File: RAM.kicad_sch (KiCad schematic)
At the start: 7 parts

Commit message: changed some ethernet stuff
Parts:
- gave numbers to parts that had none: 3
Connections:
- net USB0_D+: now also U1.A5 (USB_DP0)
- net USB0_D-: now also U1.B5 (USB_DM0)
- net USB1_D+: now also U1.B6 (USB_DP1)
- net USB1_D-: now also U1.B7 (USB_DM1)
- net USB2_D+: now also U1.A7 (USB_DP2)
- net USB2_D-: now also U1.A8 (USB_DM2)
- net USB3_D+: now also U1.B8 (USB_DP3)
- net USB3_D-: now also U1.B9 (USB_DM3)

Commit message: power things, minor changes
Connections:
- no-connect marks 10 -> 14
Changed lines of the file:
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@@
+	)
+	(no_connect
+		(at 54.61 138.43)
 	)
 	(no_connect
@@
 	)
 	(no_connect
+		(at 54.61 130.81)
+	)
+	(no_connect
 		(at 310.515 206.375)
+	)
+	(no_connect
+		(at 54.61 153.67)
 	)
 	(no_connect
@@
 	)
 	(no_connect
+		(at 54.61 208.28)
+	)
+	(no_connect

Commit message: minor changes
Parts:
- removed unit 7 of U1
- added C100, C101, C107, C108, C88, C89: 1uF, symbol Device:C
- added C102, C103, C104, C105, C109, C110, C111, C112, C113, C114, C115, C116, C117, C118, C119, C120, C121, C122, C90, C91, C92, C93, C94, C95, C96, C97, C98: 0.1uF, symbol Device:C
- added C106, C87, C99: 10uF, symbol Device:C
- added R20, R21: 2K, symbol Device:R
- added R22: 10)R, symbol Device:R
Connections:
- net GND: now also C100.2, C101.2, C102.2, C103.2, C104.2, C105.2, C106.2, C107.2, C108.2, C109.2, C110.2, C111.2, C112.2, C113.2, C114.2, C115.2, C116.2, C118.2, C119.2, C120.2, C121.2, C122.2, C87.2, C88.2, C89.2, C90.2, C91.2, C92.2, C93.2, C94.2, C95.2, C96.2, C97.2, C98.2, C99.2, R21.2
- net SCK_N: now also R22.2
- net SCK_P: now also R22.1
- net SVREF: now also C116.1, C117.2, C118.1, C119.1, C120.1, C121.1, C122.1, R20.2, R21.1
- net VCC1V5_DRAM: now also C100.1, C101.1, C102.1, C103.1, C104.1, C105.1, C106.1, C107.1, C108.1, C109.1, C110.1, C111.1, C112.1, C113.1, C114.1, C115.1, C117.1, C87.1, C88.1, C89.1, C90.1, C91.1, C92.1, C93.1, C94.1, C95.1, C96.1, C97.1, C98.1, C99.1, R20.1
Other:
- moved on the sheet: R1, R2, R3, U1C, U3, U4

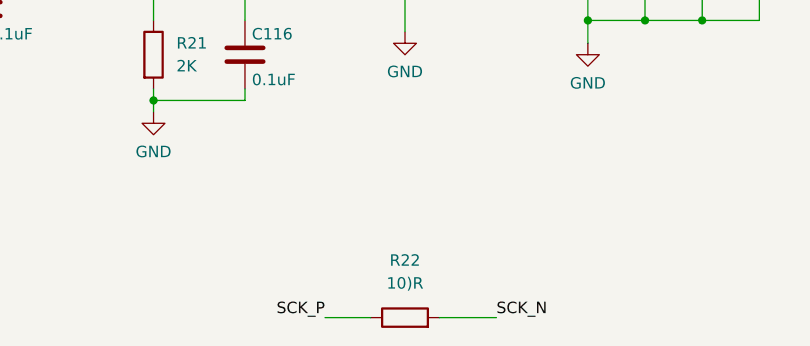
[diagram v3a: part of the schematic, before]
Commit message: linking symbols to footprints
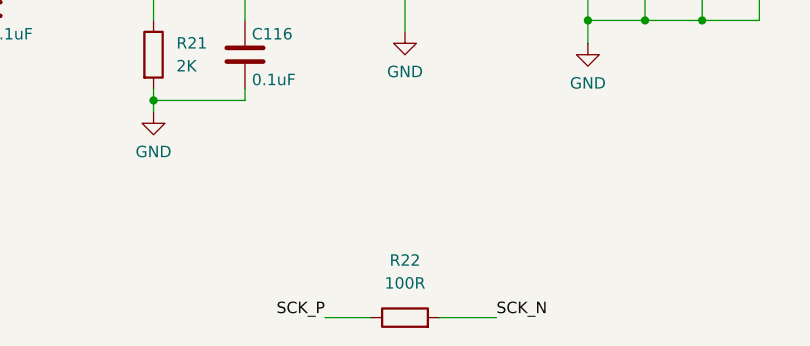
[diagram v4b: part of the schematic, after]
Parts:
- C100, C101, C107, C108, C88, C89: footprint (none) -> Capacitor_SMD:C_0402_1005Metric
- C102, C103, C104, C105, C106, C109, C110, C111, C112, C113, C114, C115, C116, C117, C118, C119, C120, C121, C122, C87, C90, C91, C92, C93, C94, C95, C96, C97, C98, C99: footprint (none) -> Capacitor_SMD:C_0603_1608Metric
- R1, R2, R20, R21, R3: footprint (none) -> Resistor_SMD:R_0402_1005Metric
- R22: value 10)R -> 100R; footprint (none) -> Resistor_SMD:R_0402_1005Metric
- U1: footprint BGA347_H3_AWT -> (none)
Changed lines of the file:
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@@
 			)
 		)
-		(property "Footprint" ""
+		(property "Footprint" "Resistor_SMD:R_0402_1005Metric"
 			(at 355.092 116.84 90)
 			(effects
@@
 			)
 		)
-		(property "Footprint" ""
+		(property "Footprint" "Capacitor_SMD:C_0603_1608Metric"
 			(at 194.0052 232.41 0)
 			(effects
@@
 			)
 		)
-		(property "Footprint" ""
+		(property "Footprint" "Capacitor_SMD:C_0603_1608Metric"
 			(at 337.5152 227.33 0)
 			(effects
@@
 			)
 		)
-		(property "Footprint" ""
+		(property "Footprint" "Capacitor_SMD:C_0603_1608Metric"
 			(at 331.1652 227.33 0)
 			(effects
@@
 			)
 		)
-		(property "Footprint" ""
+		(property "Footprint" "Capacitor_SMD:C_0603_1608Metric"
 			(at 244.8052 222.25 0)
 			(effects
@@
 			)
 		)
-		(property "Footprint" ""
+		(property "Footprint" "Capacitor_SMD:C_0402_1005Metric"
 			(at 50.4952 227.33 0)
 			(effects
@@
 			)
 		)
-		(property "Footprint" ""
+		(property "Footprint" "Capacitor_SMD:C_0603_1608Metric"
 			(at 238.4552 222.25 0)
 			(effects
@@
 			)
 		)
-		(property "Footprint" ""
+		(property "Footprint" "Capacitor_SMD:C_0603_1608Metric"
 			(at 305.7652 227.33 0)
 			(effects
@@
 			)
 		)
-		(property "Footprint" ""
+		(property "Footprint" "Capacitor_SMD:C_0603_1608Metric"
 			(at 56.8452 227.33 0)
 			(effects
@@
 			)
 		)
-		(property "Footprint" ""
+		(property "Footprint" "Resistor_SMD:R_0402_1005Metric"
 			(at 181.102 228.6 90)
 			(effects
@@
 			)
 		)
-		(property "Footprint" ""
+		(property "Footprint" "Capacitor_SMD:C_0603_1608Metric"
 			(at 107.6452 227.33 0)
 			(effects
@@
 			)
 		)
-		(property "Footprint" ""
+		(property "Footprint" "Capacitor_SMD:C_0603_1608Metric"
 			(at 101.2952 227.33 0)
 			(effects
@@
 			)
 		)
-		(property "Footprint" ""
+		(property "Footprint" "Capacitor_SMD:C_0603_1608Metric"
 			(at 324.8152 227.33 0)
 			(effects
@@
 			)
 		)
-		(property "Footprint" ""
+		(property "Footprint" "Capacitor_SMD:C_0603_1608Metric"
 			(at 251.1552 222.25 0)
 			(effects
@@
 			)
 		)
-		(property "Footprint" ""
+		(property "Footprint" "Capacitor_SMD:C_0603_1608Metric"
 			(at 312.1152 227.33 0)
 			(effects
@@
 			)
 		)
-		(property "Footprint" ""
+		(property "Footprint" "Capacitor_SMD:C_0603_1608Metric"
 			(at 88.5952 227.33 0)
 			(effects
@@
 			)
 		)
-		(property "Footprint" "BGA347_H3_AWT"
+		(property "Footprint" ""
 			(at 53.34 59.69 0)
 			(effects
@@
 			)
 		)
-		(property "Footprint" ""
+		(property "Footprint" "Capacitor_SMD:C_0603_1608Metric"
 			(at 164.7952 227.33 0)
 			(effects
@@
 			)
 		)
-		(property "Footprint" ""
+		(property "Footprint" "Capacitor_SMD:C_0603_1608Metric"
 			(at 82.2452 227.33 0)
 			(effects
@@
 			)
 		)
-		(property "Footprint" ""
+		(property "Footprint" "Resistor_SMD:R_0402_1005Metric"
 			(at 226.822 113.03 90)
 			(effects
@@
 			)
 		)
-		(property "Value" "10)R"
+		(property "Value" "100R"
 			(at 210.82 254 90)
 			(effects
@@
 			)
 		)
-		(property "Footprint" ""
+		(property "Footprint" "Resistor_SMD:R_0402_1005Metric"
 			(at 210.82 259.588 90)
 			(effects
@@
 			)
 		)
-		(property "Footprint" ""
+		(property "Footprint" "Capacitor_SMD:C_0603_1608Metric"
 			(at 63.1952 227.33 0)
 			(effects
@@
 			)
 		)
-		(property "Footprint" ""
+		(property "Footprint" "Capacitor_SMD:C_0402_1005Metric"
 			(at 44.1452 227.33 0)
 			(effects
@@
 			)
 		)
-		(property "Footprint" ""
+		(property "Footprint" "Capacitor_SMD:C_0402_1005Metric"
 			(at 299.4152 227.33 0)
 			(effects
@@
 			)
 		)
-		(property "Footprint" ""
+		(property "Footprint" "Capacitor_SMD:C_0603_1608Metric"
 			(at 211.7852 220.98 0)
 			(effects
@@
 			)
 		)
-		(property "Footprint" ""
+		(property "Footprint" "Capacitor_SMD:C_0603_1608Metric"
 			(at 75.8952 227.33 0)
 			(effects
@@
 			)
 		)
-		(property "Footprint" ""
+		(property "Footprint" "Resistor_SMD:R_0402_1005Metric"
 			(at 181.102 213.36 90)
 			(effects
@@
 			)
 		)
-		(property "Footprint" ""
+		(property "Footprint" "Capacitor_SMD:C_0603_1608Metric"
 			(at 343.8652 227.33 0)
 			(effects
@@
 			)
 		)
-		(property "Footprint" ""
+		(property "Footprint" "Capacitor_SMD:C_0603_1608Metric"
 			(at 194.0052 217.17 0)
 			(effects
@@
 			)
 		)
-		(property "Footprint" ""
+		(property "Footprint" "Capacitor_SMD:C_0603_1608Metric"
 			(at 158.4452 227.33 0)
 			(effects
@@
 			)
 		)
-		(property "Footprint" ""
+		(property "Footprint" "Capacitor_SMD:C_0603_1608Metric"
 			(at 318.4652 227.33 0)
 			(effects
@@
 			)
 		)
-		(property "Footprint" ""
+		(property "Footprint" "Capacitor_SMD:C_0603_1608Metric"
 			(at 232.1052 222.25 0)
 			(effects
@@
 			)
 		)
-		(property "Footprint" ""
+		(property "Footprint" "Capacitor_SMD:C_0603_1608Metric"
 			(at 286.7152 227.33 0)
 			(effects
@@
 			)
 		)
-		(property "Footprint" ""
+		(property "Footprint" "Capacitor_SMD:C_0603_1608Metric"
 			(at 126.6952 227.33 0)
 			(effects
@@
 			)
 		)
-		(property "Footprint" ""
+		(property "Footprint" "Capacitor_SMD:C_0402_1005Metric"
 			(at 133.0452 227.33 0)
 			(effects
@@
 			)
 		)
-		(property "Footprint" ""
+		(property "Footprint" "Capacitor_SMD:C_0603_1608Metric"
 			(at 152.0952 227.33 0)
 			(effects
@@
 			)
 		)
-		(property "Footprint" ""
+		(property "Footprint" "Resistor_SMD:R_0402_1005Metric"
 			(at 45.72 57.912 90)
 			(effects
@@
 			)
 		)
-		(property "Footprint" ""
+		(property "Footprint" "Capacitor_SMD:C_0603_1608Metric"
 			(at 145.7452 227.33 0)
 			(effects
@@
 			)
 		)
-		(property "Footprint" ""
+		(property "Footprint" "Capacitor_SMD:C_0603_1608Metric"
 			(at 94.9452 227.33 0)
 			(effects
@@
 			)
 		)
-		(property "Footprint" ""
+		(property "Footprint" "Capacitor_SMD:C_0402_1005Metric"
 			(at 139.3952 227.33 0)
 			(effects
@@
 			)
 		)
-		(property "Footprint" ""
+		(property "Footprint" "Capacitor_SMD:C_0402_1005Metric"
 			(at 293.0652 227.33 0)
 			(effects
@@
 			)
 		)
-		(property "Footprint" ""
+		(property "Footprint" "Capacitor_SMD:C_0603_1608Metric"
 			(at 37.7952 227.33 0)
 			(effects
@@
 			)
 		)
-		(property "Footprint" ""
+		(property "Footprint" "Capacitor_SMD:C_0603_1608Metric"
 			(at 69.5452 227.33 0)
 			(effects

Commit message: placed major components
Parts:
- C102, C103, C104, C105, C106, C109, C110, C111, C112, C113, C114, C115, C116, C117, C118, C119, C120, C121, C122, C87, C90, C91, C92, C93, C94, C95, C96, C97, C98, C99: footprint Capacitor_SMD:C_0603_1608Metric -> Capacitor_SMD:C_0402_1005Metric
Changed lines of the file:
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@@
 			)
 		)
-		(property "Footprint" "Capacitor_SMD:C_0603_1608Metric"
+		(property "Footprint" "Capacitor_SMD:C_0402_1005Metric"
 			(at 194.0052 232.41 0)
 			(effects
@@
 			)
 		)
-		(property "Footprint" "Capacitor_SMD:C_0603_1608Metric"
+		(property "Footprint" "Capacitor_SMD:C_0402_1005Metric"
 			(at 337.5152 227.33 0)
 			(effects
@@
 			)
 		)
-		(property "Footprint" "Capacitor_SMD:C_0603_1608Metric"
+		(property "Footprint" "Capacitor_SMD:C_0402_1005Metric"
 			(at 331.1652 227.33 0)
 			(effects
@@
 			)
 		)
-		(property "Footprint" "Capacitor_SMD:C_0603_1608Metric"
+		(property "Footprint" "Capacitor_SMD:C_0402_1005Metric"
 			(at 244.8052 222.25 0)
 			(effects
@@
 			)
 		)
-		(property "Footprint" "Capacitor_SMD:C_0603_1608Metric"
+		(property "Footprint" "Capacitor_SMD:C_0402_1005Metric"
 			(at 238.4552 222.25 0)
 			(effects
@@
 			)
 		)
-		(property "Footprint" "Capacitor_SMD:C_0603_1608Metric"
+		(property "Footprint" "Capacitor_SMD:C_0402_1005Metric"
 			(at 305.7652 227.33 0)
 			(effects
@@
 			)
 		)
-		(property "Footprint" "Capacitor_SMD:C_0603_1608Metric"
+		(property "Footprint" "Capacitor_SMD:C_0402_1005Metric"
 			(at 56.8452 227.33 0)
 			(effects
@@
 			)
 		)
-		(property "Footprint" "Capacitor_SMD:C_0603_1608Metric"
+		(property "Footprint" "Capacitor_SMD:C_0402_1005Metric"
 			(at 107.6452 227.33 0)
 			(effects
@@
 			)
 		)
-		(property "Footprint" "Capacitor_SMD:C_0603_1608Metric"
+		(property "Footprint" "Capacitor_SMD:C_0402_1005Metric"
 			(at 101.2952 227.33 0)
 			(effects
@@
 			)
 		)
-		(property "Footprint" "Capacitor_SMD:C_0603_1608Metric"
+		(property "Footprint" "Capacitor_SMD:C_0402_1005Metric"
 			(at 324.8152 227.33 0)
 			(effects
@@
 			)
 		)
-		(property "Footprint" "Capacitor_SMD:C_0603_1608Metric"
+		(property "Footprint" "Capacitor_SMD:C_0402_1005Metric"
 			(at 251.1552 222.25 0)
 			(effects
@@
 			)
 		)
-		(property "Footprint" "Capacitor_SMD:C_0603_1608Metric"
+		(property "Footprint" "Capacitor_SMD:C_0402_1005Metric"
 			(at 312.1152 227.33 0)
 			(effects
@@
 			)
 		)
-		(property "Footprint" "Capacitor_SMD:C_0603_1608Metric"
+		(property "Footprint" "Capacitor_SMD:C_0402_1005Metric"
 			(at 88.5952 227.33 0)
 			(effects
@@
 			)
 		)
-		(property "Footprint" "Capacitor_SMD:C_0603_1608Metric"
+		(property "Footprint" "Capacitor_SMD:C_0402_1005Metric"
 			(at 164.7952 227.33 0)
 			(effects
@@
 			)
 		)
-		(property "Footprint" "Capacitor_SMD:C_0603_1608Metric"
+		(property "Footprint" "Capacitor_SMD:C_0402_1005Metric"
 			(at 82.2452 227.33 0)
 			(effects
@@
 			)
 		)
-		(property "Footprint" "Capacitor_SMD:C_0603_1608Metric"
+		(property "Footprint" "Capacitor_SMD:C_0402_1005Metric"
 			(at 63.1952 227.33 0)
 			(effects
@@
 			)
 		)
-		(property "Footprint" "Capacitor_SMD:C_0603_1608Metric"
+		(property "Footprint" "Capacitor_SMD:C_0402_1005Metric"
 			(at 211.7852 220.98 0)
 			(effects
@@
 			)
 		)
-		(property "Footprint" "Capacitor_SMD:C_0603_1608Metric"
+		(property "Footprint" "Capacitor_SMD:C_0402_1005Metric"
 			(at 75.8952 227.33 0)
 			(effects
@@
 			)
 		)
-		(property "Footprint" "Capacitor_SMD:C_0603_1608Metric"
+		(property "Footprint" "Capacitor_SMD:C_0402_1005Metric"
 			(at 343.8652 227.33 0)
 			(effects
@@
 			)
 		)
-		(property "Footprint" "Capacitor_SMD:C_0603_1608Metric"
+		(property "Footprint" "Capacitor_SMD:C_0402_1005Metric"
 			(at 194.0052 217.17 0)
 			(effects
@@
 			)
 		)
-		(property "Footprint" "Capacitor_SMD:C_0603_1608Metric"
+		(property "Footprint" "Capacitor_SMD:C_0402_1005Metric"
 			(at 158.4452 227.33 0)
 			(effects
@@
 			)
 		)
-		(property "Footprint" "Capacitor_SMD:C_0603_1608Metric"
+		(property "Footprint" "Capacitor_SMD:C_0402_1005Metric"
 			(at 318.4652 227.33 0)
 			(effects
@@
 			)
 		)
-		(property "Footprint" "Capacitor_SMD:C_0603_1608Metric"
+		(property "Footprint" "Capacitor_SMD:C_0402_1005Metric"
 			(at 232.1052 222.25 0)
 			(effects
@@
 			)
 		)
-		(property "Footprint" "Capacitor_SMD:C_0603_1608Metric"
+		(property "Footprint" "Capacitor_SMD:C_0402_1005Metric"
 			(at 286.7152 227.33 0)
 			(effects
@@
 			)
 		)
-		(property "Footprint" "Capacitor_SMD:C_0603_1608Metric"
+		(property "Footprint" "Capacitor_SMD:C_0402_1005Metric"
 			(at 126.6952 227.33 0)
 			(effects
@@
 			)
 		)
-		(property "Footprint" "Capacitor_SMD:C_0603_1608Metric"
+		(property "Footprint" "Capacitor_SMD:C_0402_1005Metric"
 			(at 152.0952 227.33 0)
 			(effects
@@
 			)
 		)
-		(property "Footprint" "Capacitor_SMD:C_0603_1608Metric"
+		(property "Footprint" "Capacitor_SMD:C_0402_1005Metric"
 			(at 145.7452 227.33 0)
 			(effects
@@
 			)
 		)
-		(property "Footprint" "Capacitor_SMD:C_0603_1608Metric"
+		(property "Footprint" "Capacitor_SMD:C_0402_1005Metric"
 			(at 94.9452 227.33 0)
 			(effects
@@
 			)
 		)
-		(property "Footprint" "Capacitor_SMD:C_0603_1608Metric"
+		(property "Footprint" "Capacitor_SMD:C_0402_1005Metric"
 			(at 37.7952 227.33 0)
 			(effects
@@
 			)
 		)
-		(property "Footprint" "Capacitor_SMD:C_0603_1608Metric"
+		(property "Footprint" "Capacitor_SMD:C_0402_1005Metric"
 			(at 69.5452 227.33 0)
 			(effects

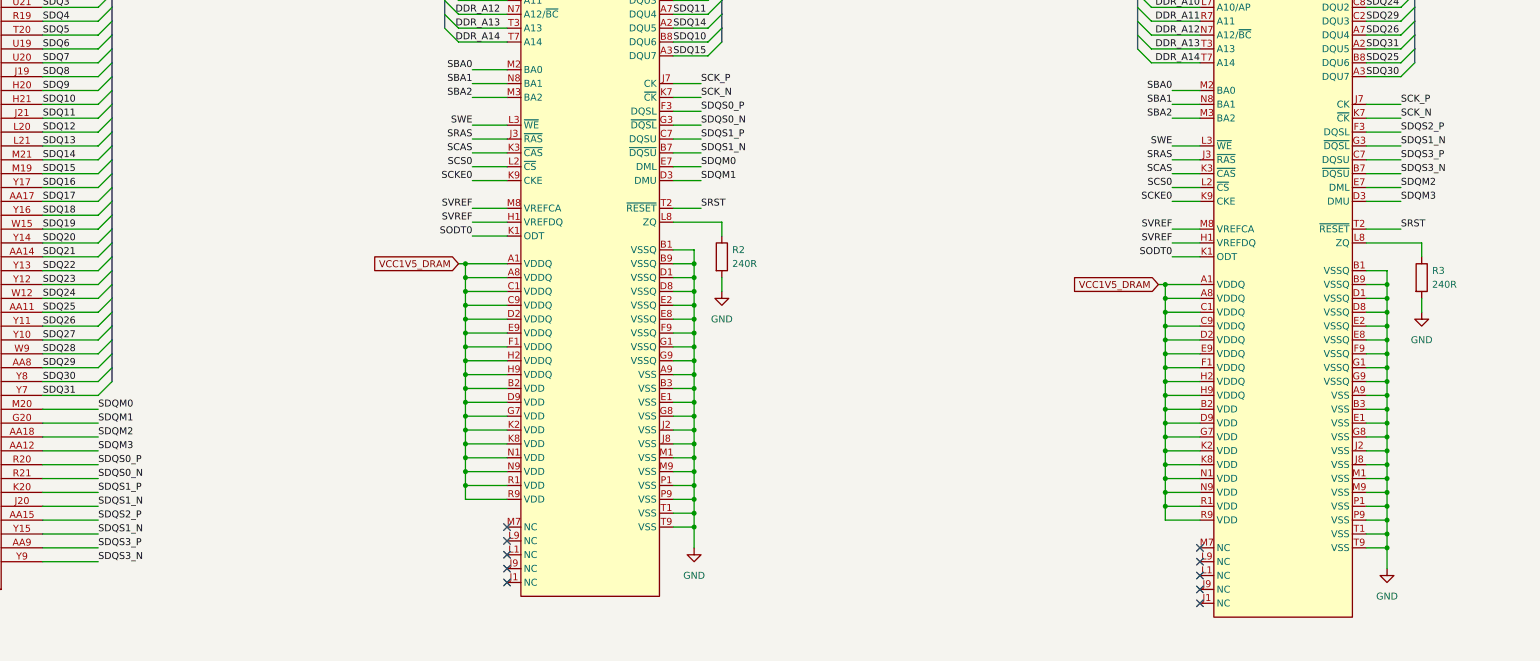
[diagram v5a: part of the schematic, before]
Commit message: started RAM routing, might move to 1 module though
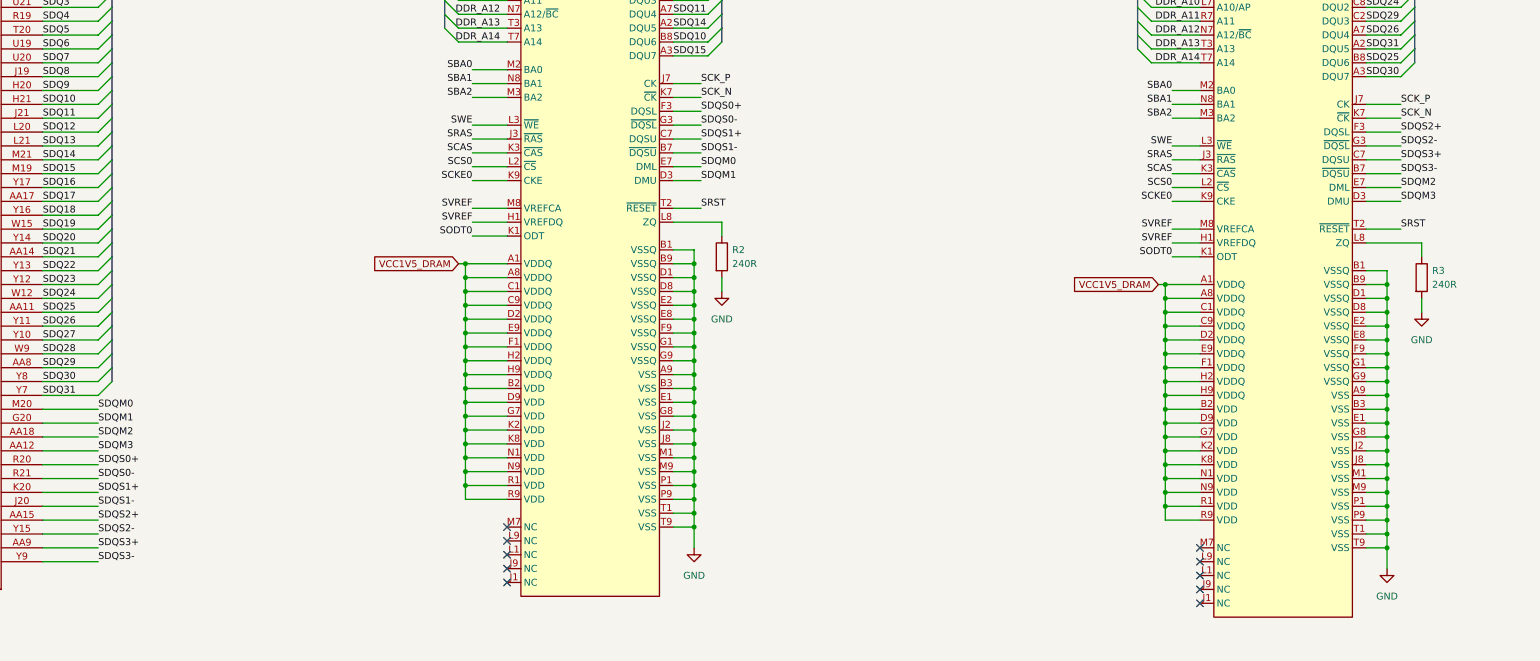
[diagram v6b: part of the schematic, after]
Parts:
- U1: footprint (none) -> easyeda2kicad:BGA-347_L14.0-W14.0-R21-C21-P0.65-TL
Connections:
- net SDQS0_N renamed SDQS0-
- net SDQS0_P renamed SDQS0+
- net SDQS1_N renamed SDQS1-
- net SDQS1-: no longer U1.Y15 (SDQS2B), U4.G3 (~{DQSL})
- net SDQS1_P renamed SDQS1+
- net SDQS2_P renamed SDQS2+
- net SDQS3_N renamed SDQS3-
- net SDQS3_P renamed SDQS3+
- new net SDQS2-: U1.Y15 (SDQS2B), U4.G3 (~{DQSL})
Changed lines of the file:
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@@
 		)
 	)
-	(label "SDQS2_P"
+	(label "SDQS2+"
 		(at 353.06 90.17 0)
 		(effects
@@
 		)
 	)
-	(label "SDQS3_N"
+	(label "SDQS3-"
 		(at 114.3 168.91 0)
 		(effects
@@
 		)
 	)
-	(label "SDQS1_N"
+	(label "SDQS2-"
 		(at 114.3 163.83 0)
 		(effects
@@
 		)
 	)
-	(label "SDQS1_P"
+	(label "SDQS1+"
 		(at 224.79 91.44 0)
 		(effects
@@
 		)
 	)
-	(label "SDQS1_P"
+	(label "SDQS1+"
 		(at 114.3 156.21 0)
 		(effects
@@
 			(justify left bottom)
 		)
+		(property "Netclass" "DDR0_DQL"
+			(at 219.71 39.37 0)
+			(effects
+				(font
+					(size 1.27 1.27)
+					(italic yes)
+				)
+				(justify left)
+				(hide yes)
+			)
+		)
 	)
 	(label "SDQ29"
@@
 		)
 	)
-	(label "SDQS1_N"
+	(label "SDQS2-"
 		(at 353.06 92.71 0)
 		(effects
@@
 		)
 	)
-	(label "SDQS0_P"
+	(label "SDQS0+"
 		(at 114.3 151.13 0)
 		(effects
@@
 		)
 	)
-	(label "SDQS3_P"
+	(label "SDQS3+"
 		(at 353.06 95.25 0)
 		(effects
@@
 		)
 	)
-	(label "SDQS2_P"
+	(label "SDQS2+"
 		(at 114.3 161.29 0)
 		(effects
@@
 		)
 	)
-	(label "SDQS3_N"
+	(label "SDQS3-"
 		(at 353.06 97.79 0)
 		(effects
@@
 		)
 	)
-	(label "SDQS1_N"
+	(label "SDQS1-"
 		(at 114.3 158.75 0)
 		(effects
@@
 		)
 	)
-	(label "SDQS0_P"
+	(label "SDQS0+"
 		(at 224.79 86.36 0)
 		(effects
@@
 		)
 	)
-	(label "SDQS1_N"
+	(label "SDQS1-"
 		(at 224.79 93.98 0)
 		(effects
@@
 		)
 	)
-	(label "SDQS3_P"
+	(label "SDQS3+"
 		(at 114.3 166.37 0)
 		(effects
@@
 		)
 	)
-	(label "SDQS0_N"
+	(label "SDQS0-"
 		(at 114.3 153.67 0)
 		(effects
@@
 		)
 	)
-	(label "SDQS0_N"
+	(label "SDQS0-"
 		(at 224.79 88.9 0)
 		(effects
@@
 		)
 	)
+	(rule_area
+		(polyline
+			(pts
+				(xy 189.23 34.29) (xy 189.23 74.93) (xy 179.07 74.93) (xy 179.07 34.29)
+			)
+			(stroke
+				(width 0)
+				(type dash)
+			)
+			(fill
+				(type none)
+			)
+		)
+	)
+	(netclass_flag ""
+		(length 2.54)
+		(shape round)
+		(at 179.07 34.29 0)
+		(fields_autoplaced yes)
+		(effects
+			(font
+				(size 1.27 1.27)
+			)
+			(justify left bottom)
+		)
+		(property "Netclass" "DDR0_ADDR"
+			(at 179.7685 31.75 0)
+			(effects
+				(font
+					(size 1.27 1.27)
+				)
+				(justify left)
+			)
+		)
+		(property "Component Class" ""
+			(at -72.39 -21.59 0)
+			(effects
+				(font
+					(size 1.27 1.27)
+					(italic yes)
+				)
+			)
+		)
+	)
 	(symbol
 		(lib_id "Device:R")
@@
 			)
 		)
-		(property "Footprint" ""
+		(property "Footprint" "easyeda2kicad:BGA-347_L14.0-W14.0-R21-C21-P0.65-TL"
 			(at 53.34 59.69 0)
 			(effects
